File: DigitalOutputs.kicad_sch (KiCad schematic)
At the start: 2 parts, among them J3 DIGITAL_OUTPUTS

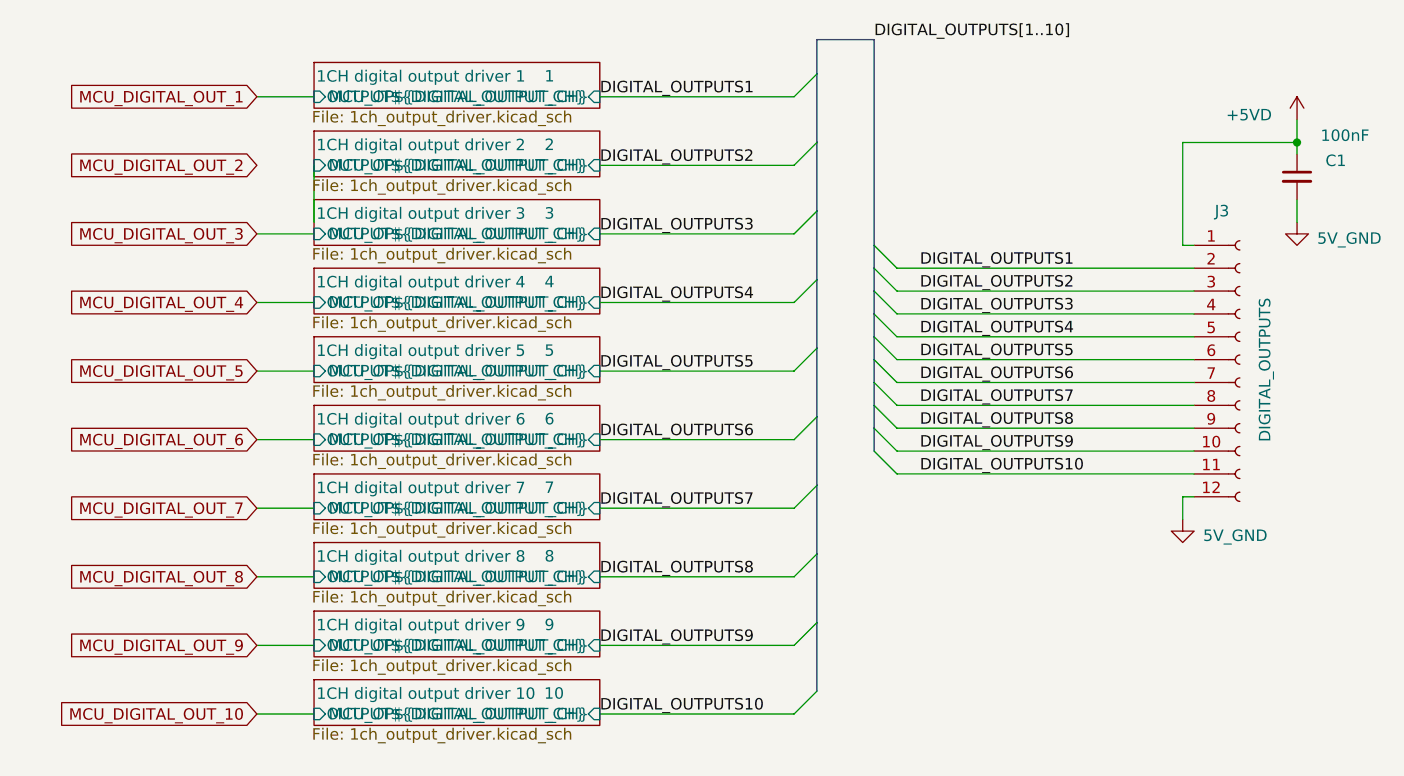
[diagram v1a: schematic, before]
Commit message: digital inputs section
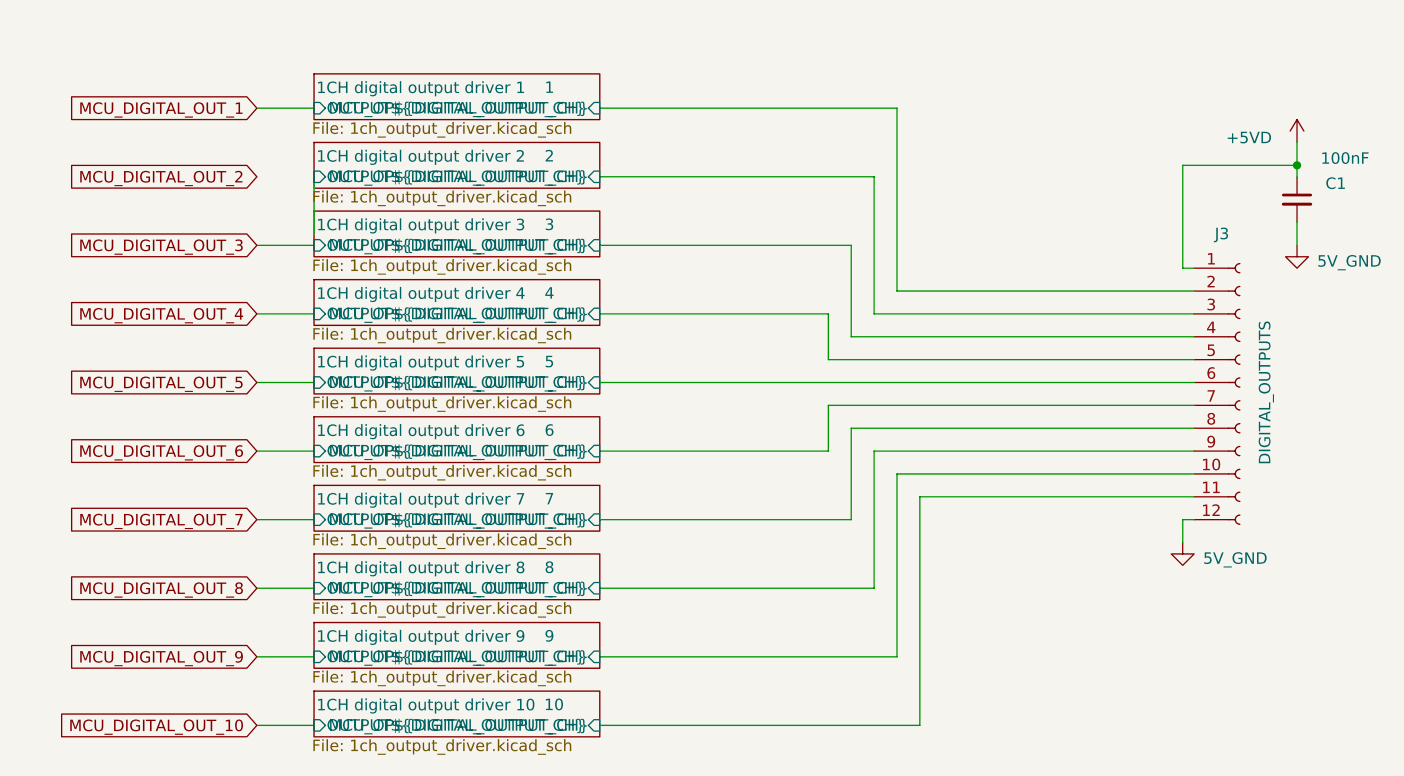
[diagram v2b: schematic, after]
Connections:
- net DIGITAL_OUTPUTS1 renamed 1CH digital output driver 1/OUTPUT${DIGITAL_OUTPUT_CH}
- net DIGITAL_OUTPUTS10 renamed 1CH digital output driver 10/OUTPUT${DIGITAL_OUTPUT_CH}
- net DIGITAL_OUTPUTS2 renamed 1CH digital output driver 2/OUTPUT${DIGITAL_OUTPUT_CH}
- net DIGITAL_OUTPUTS3 renamed 1CH digital output driver 3/OUTPUT${DIGITAL_OUTPUT_CH}
- net DIGITAL_OUTPUTS4 renamed 1CH digital output driver 4/OUTPUT${DIGITAL_OUTPUT_CH}
- net DIGITAL_OUTPUTS5 renamed 1CH digital output driver 5/OUTPUT${DIGITAL_OUTPUT_CH}
- net DIGITAL_OUTPUTS6 renamed 1CH digital output driver 6/OUTPUT${DIGITAL_OUTPUT_CH}
- net DIGITAL_OUTPUTS7 renamed 1CH digital output driver 7/OUTPUT${DIGITAL_OUTPUT_CH}
- net DIGITAL_OUTPUTS8 renamed 1CH digital output driver 8/OUTPUT${DIGITAL_OUTPUT_CH}
- net DIGITAL_OUTPUTS9 renamed 1CH digital output driver 9/OUTPUT${DIGITAL_OUTPUT_CH}
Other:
- moved on the sheet: C1, J3

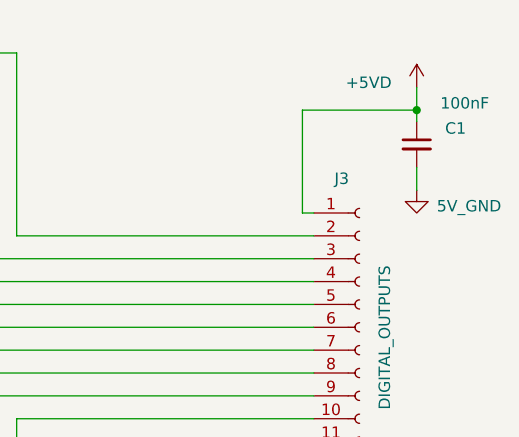
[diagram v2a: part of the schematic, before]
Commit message: Deleted stale test production files. Fixed up a bug with power isolation. Created some footprints for wire to board connectors although ran out of time to fix a bug where they do no lock in. Fixes to readme
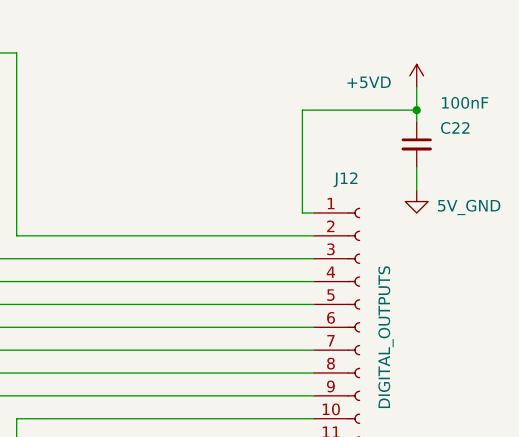
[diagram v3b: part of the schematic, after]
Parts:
- J12: renamed from J3; footprint (none) -> OSTVTerminalBlocks:Conn01x12
- renumbered C1 to C22
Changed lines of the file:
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@@
 		(on_board yes)
 		(dnp no)
-		(property "Reference" "C1"
+		(property "Reference" "C22"
 			(at 216.408 74.422 0)
 			(effects
@@
 			(project "Remora Nucleo F446ZE Hat"
 				(path "/5473abc6-7b93-43cc-a401-f691c4d7d7cf/a10f9653-3098-46b3-8571-958500eea49a"
-					(reference "C1")
+					(reference "C22")
 					(unit 1)
 				)
@@
 		(on_board yes)
 		(dnp no)
-		(property "Reference" "#PWR0136"
+		(property "Reference" "#PWR0135"
 			(at 199.39 120.65 0)
 			(effects
@@
 			(project "Remora Nucleo F446ZE Hat"
 				(path "/5473abc6-7b93-43cc-a401-f691c4d7d7cf/a10f9653-3098-46b3-8571-958500eea49a"
-					(reference "#PWR0136")
+					(reference "#PWR0135")
 					(unit 1)
 				)
@@
 		(on_board yes)
 		(dnp no)
-		(property "Reference" "#PWR0135"
+		(property "Reference" "#PWR0136"
 			(at 212.09 73.66 0)
 			(effects
@@
 			(project "Remora Nucleo F446ZE Hat"
 				(path "/5473abc6-7b93-43cc-a401-f691c4d7d7cf/a10f9653-3098-46b3-8571-958500eea49a"
-					(reference "#PWR0135")
+					(reference "#PWR0136")
 					(unit 1)
 				)
@@
 		(on_board yes)
 		(dnp no)
-		(property "Reference" "J3"
+		(property "Reference" "J12"
 			(at 202.946 80.01 0)
 			(effects
@@
 			)
 		)
-		(property "Footprint" ""
+		(property "Footprint" "OSTVTerminalBlocks:Conn01x12"
 			(at 205.74 96.52 0)
 			(effects
@@
 			(project "Remora Nucleo F446ZE Hat"
 				(path "/5473abc6-7b93-43cc-a401-f691c4d7d7cf/a10f9653-3098-46b3-8571-958500eea49a"
-					(reference "J3")
-					(unit 1)
-				)
+					(reference "J12")
+					(unit 1)
+				)

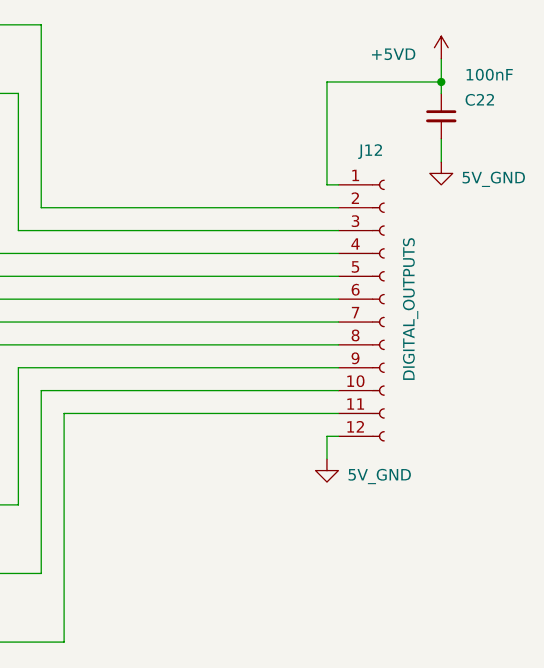
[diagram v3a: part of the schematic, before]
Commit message: restructured power supplies to enable Spindle DAC to be isolated. We now have the option of supplying two 24V inputs, one to power the nucleo and everything logic side and the other to power peripherals. Some testing will be required.
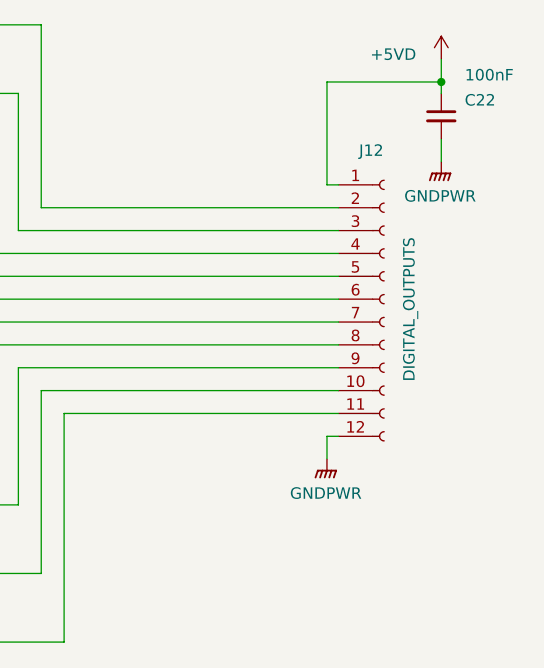
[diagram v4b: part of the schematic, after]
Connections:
- net 5V_GND renamed GNDPWR
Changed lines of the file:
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@@
 	)
 	(symbol
-		(lib_id "power:GND1")
+		(lib_id "power:GNDPWR")
 		(at 212.09 81.28 0)
 		(unit 1)
@@
 		(on_board yes)
 		(dnp no)
-		(property "Reference" "#PWR0137"
-			(at 212.09 87.63 0)
-			(effects
-				(font
-					(size 1.27 1.27)
-				)
-				(hide yes)
-			)
-		)
-		(property "Value" "5V_GND"
-			(at 221.488 83.058 0)
-			(effects
-				(font
-					(size 1.27 1.27)
-				)
-				(justify right)
+		(fields_autoplaced yes)
+		(property "Reference" "#PWR0117"
+			(at 212.09 86.36 0)
+			(effects
+				(font
+					(size 1.27 1.27)
+				)
+				(hide yes)
+			)
+		)
+		(property "Value" "GNDPWR"
+			(at 211.963 85.09 0)
+			(effects
+				(font
+					(size 1.27 1.27)
+				)
 			)
 		)
 		(property "Footprint" ""
+			(at 212.09 82.55 0)
+			(effects
+				(font
+					(size 1.27 1.27)
+				)
+				(hide yes)
+			)
+		)
+		(property "Datasheet" ""
+			(at 212.09 82.55 0)
+			(effects
+				(font
+					(size 1.27 1.27)
+				)
+				(hide yes)
+			)
+		)
+		(property "Description" "Power symbol creates a global label with name \"GNDPWR\" , global ground"
 			(at 212.09 81.28 0)
 			(effects
@@
 			)
 		)
-		(property "Datasheet" ""
-			(at 212.09 81.28 0)
-			(effects
-				(font
-					(size 1.27 1.27)
-				)
-				(hide yes)
-			)
-		)
-		(property "Description" "Power symbol creates a global label with name \"GND1\" , ground"
-			(at 212.09 81.28 0)
-			(effects
-				(font
-					(size 1.27 1.27)
-				)
-				(hide yes)
-			)
-		)
-		(pin "1"
-		)
-		(instances
-			(project "Remora Nucleo F446ZE Hat"
-				(path "/5473abc6-7b93-43cc-a401-f691c4d7d7cf/a10f9653-3098-46b3-8571-958500eea49a"
-					(reference "#PWR0137")
-					(unit 1)
-				)
-			)
-		)
-	)
-	(symbol
-		(lib_id "power:GND1")
-		(at 199.39 114.3 0)
-		(unit 1)
-		(exclude_from_sim no)
-		(in_bom yes)
-		(on_board yes)
-		(dnp no)
-		(property "Reference" "#PWR0135"
-			(at 199.39 120.65 0)
-			(effects
-				(font
-					(size 1.27 1.27)
-				)
-				(hide yes)
-			)
-		)
-		(property "Value" "5V_GND"
-			(at 205.232 116.078 0)
-			(effects
-				(font
-					(size 1.27 1.27)
-				)
-			)
-		)
-		(property "Footprint" ""
-			(at 199.39 114.3 0)
-			(effects
-				(font
-					(size 1.27 1.27)
-				)
-				(hide yes)
-			)
-		)
-		(property "Datasheet" ""
-			(at 199.39 114.3 0)
-			(effects
-				(font
-					(size 1.27 1.27)
-				)
-				(hide yes)
-			)
-		)
-		(property "Description" "Power symbol creates a global label with name \"GND1\" , ground"
-			(at 199.39 114.3 0)
-			(effects
-				(font
-					(size 1.27 1.27)
-				)
-				(hide yes)
-			)
-		)
-		(pin "1"
-		)
-		(instances
-			(project "Remora Nucleo F446ZE Hat"
-				(path "/5473abc6-7b93-43cc-a401-f691c4d7d7cf/a10f9653-3098-46b3-8571-958500eea49a"
-					(reference "#PWR0135")
+		(pin "1"
+		)
+		(instances
+			(project "Remora Nucleo F446ZE Hat"
+				(path "/5473abc6-7b93-43cc-a401-f691c4d7d7cf/a10f9653-3098-46b3-8571-958500eea49a"
+					(reference "#PWR0117")
 					(unit 1)
 				)
@@
 					(unit 1)
 				)
+			)
+		)
+	)
+	(symbol
+		(lib_id "power:GNDPWR")
+		(at 199.39 114.3 0)
+		(unit 1)
+		(exclude_from_sim no)
+		(in_bom yes)
+		(on_board yes)
+		(dnp no)
+		(fields_autoplaced yes)
+		(property "Reference" "#PWR0113"
+			(at 199.39 119.38 0)
+			(effects
+				(font
+					(size 1.27 1.27)
+				)
+				(hide yes)
+			)
+		)
+		(property "Value" "GNDPWR"
+			(at 199.263 118.11 0)
+			(effects
+				(font
+					(size 1.27 1.27)
+				)
+			)
+		)
+		(property "Footprint" ""
+			(at 199.39 115.57 0)
+			(effects
+				(font
+					(size 1.27 1.27)
+				)
+				(hide yes)
+			)
+		)
+		(property "Datasheet" ""
+			(at 199.39 115.57 0)
+			(effects
+				(font
+					(size 1.27 1.27)
+				)
+				(hide yes)
+			)
+		)
+		(property "Description" "Power symbol creates a global label with name \"GNDPWR\" , global ground"
+			(at 199.39 114.3 0)
+			(effects
+				(font
+					(size 1.27 1.27)
+				)
+				(hide yes)
+			)
+		)
+		(pin "1"
+		)
+		(instances
+			(project "Remora Nucleo F446ZE Hat"
+				(path "/5473abc6-7b93-43cc-a401-f691c4d7d7cf/a10f9653-3098-46b3-8571-958500eea49a"
+					(reference "#PWR0113")
+					(unit 1)
+				)

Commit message: Fixes to screw terminal footprints, updated BOM and included in project folder
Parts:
- J12: footprint OSTVTerminalBlocks:Conn01x12 -> EBWA_06_A:CONN_EBWA-12-A_ADM
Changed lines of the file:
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@@
 			)
 		)
-		(property "Footprint" "OSTVTerminalBlocks:Conn01x12"
+		(property "Footprint" "EBWA_06_A:CONN_EBWA-12-A_ADM"
 			(at 205.74 96.52 0)
 			(effects

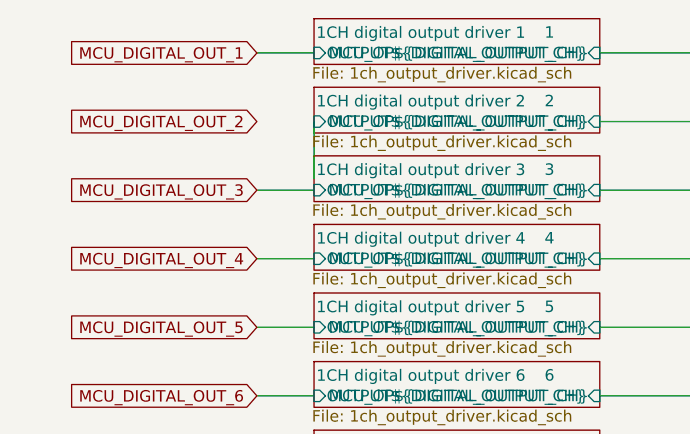
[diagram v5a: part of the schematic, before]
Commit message: Fixed bug with lack of pin header for CN11 and CN12. Addeded RPI header and aligned it, assigned some safe footprints
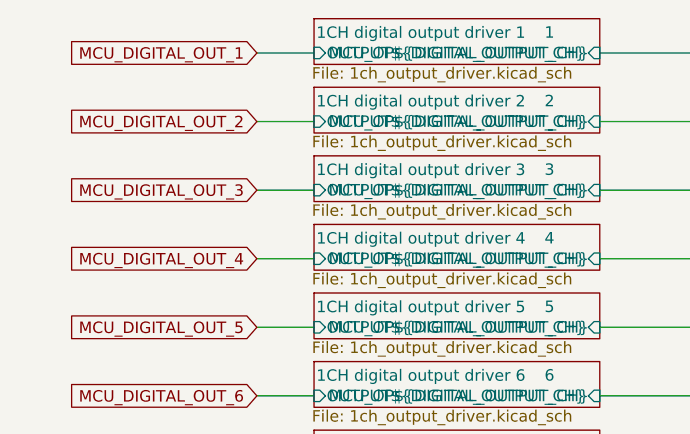
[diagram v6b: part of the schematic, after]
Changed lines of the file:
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@@
+	(wire
+		(pts
+			(xy 96.52 73.66) (xy 102.87 73.66)
+		)
+		(stroke
+			(width 0)
+			(type default)
+		)
+	)
 	(wire
 		(pts
@@
 		)
 		(stroke
-			(width 0)
-			(type default)
-		)
-	)
-	(wire
-		(pts
-			(xy 102.87 80.01) (xy 102.87 73.66)
-		)
-		(stroke

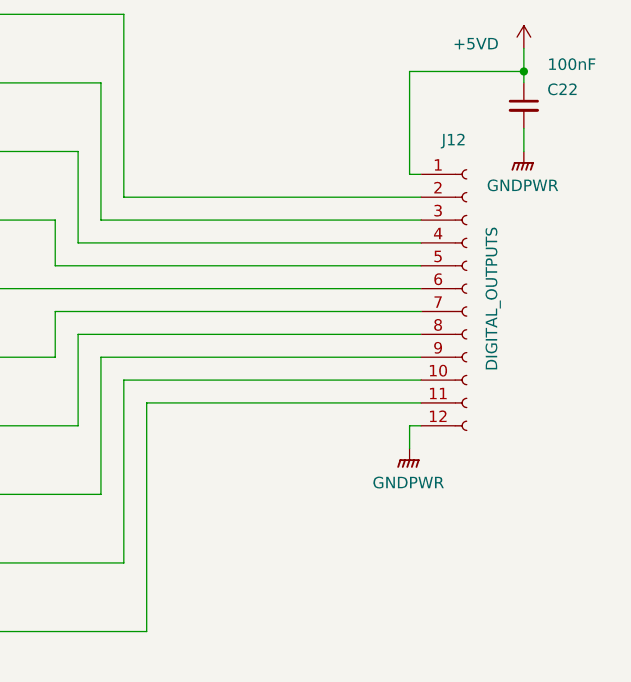
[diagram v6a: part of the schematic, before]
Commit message: updates to read me, marked V1 parts inactive and made start on board layout for initial test board. fixes to BOM to suit
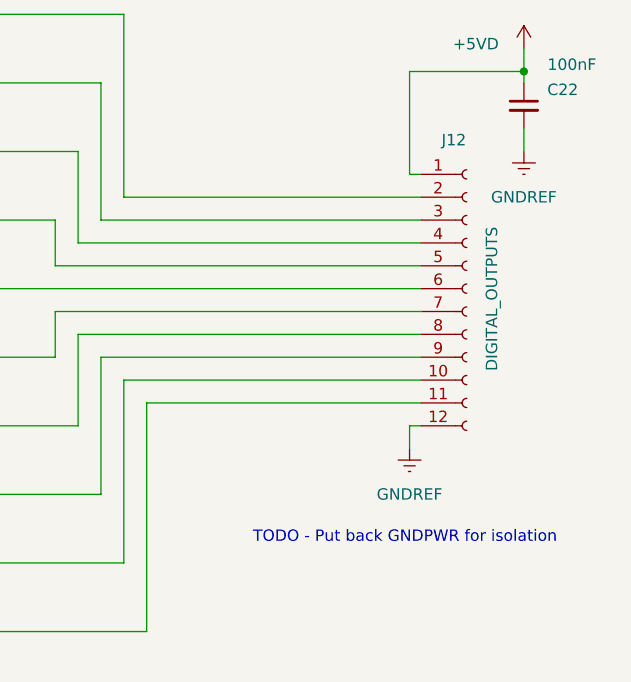
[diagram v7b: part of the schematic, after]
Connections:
- net GNDPWR renamed GNDREF
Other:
- note added: "TODO - Put back GNDPWR for isolation"
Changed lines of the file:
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@@
 	(generator_version "9.0")
 	(paper "A4")
+	(text "TODO - Put back GNDPWR for isolation\n"
+		(exclude_from_sim no)
+		(at 198.882 124.206 0)
+		(effects
+			(font
+				(size 1.27 1.27)
+			)
+		)
+	)
 	(junction
 		(at 212.09 72.39)
@@
 				(justify right)
 				(hide yes)
+			)
+		)
+	)
+	(symbol
+		(lib_id "power:GNDREF")
+		(at 199.39 114.3 0)
+		(unit 1)
+		(exclude_from_sim no)
+		(in_bom yes)
+		(on_board yes)
+		(dnp no)
+		(fields_autoplaced yes)
+		(property "Reference" "#PWR0117"
+			(at 199.39 120.65 0)
+			(effects
+				(font
+					(size 1.27 1.27)
+				)
+				(hide yes)
+			)
+		)
+		(property "Value" "GNDREF"
+			(at 199.39 119.38 0)
+			(effects
+				(font
+					(size 1.27 1.27)
+				)
+			)
+		)
+		(property "Footprint" ""
+			(at 199.39 114.3 0)
+			(effects
+				(font
+					(size 1.27 1.27)
+				)
+				(hide yes)
+			)
+		)
+		(property "Datasheet" ""
+			(at 199.39 114.3 0)
+			(effects
+				(font
+					(size 1.27 1.27)
+				)
+				(hide yes)
+			)
+		)
+		(property "Description" "Power symbol creates a global label with name \"GNDREF\" , reference supply ground"
+			(at 199.39 114.3 0)
+			(effects
+				(font
+					(size 1.27 1.27)
+				)
+				(hide yes)
+			)
+		)
+		(pin "1"
+		)
+		(instances
+			(project "Remora Nucleo F446ZE Hat"
+				(path "/5473abc6-7b93-43cc-a401-f691c4d7d7cf/a10f9653-3098-46b3-8571-958500eea49a"
+					(reference "#PWR0117")
+					(unit 1)
+				)
 			)
 		)
@@
 	)
 	(symbol
-		(lib_id "power:GNDPWR")
+		(lib_id "power:GNDREF")
 		(at 212.09 81.28 0)
 		(unit 1)
@@
 		(dnp no)
 		(fields_autoplaced yes)
-		(property "Reference" "#PWR0117"
+		(property "Reference" "#PWR0113"
+			(at 212.09 87.63 0)
+			(effects
+				(font
+					(size 1.27 1.27)
+				)
+				(hide yes)
+			)
+		)
+		(property "Value" "GNDREF"
 			(at 212.09 86.36 0)
 			(effects
@@
 					(size 1.27 1.27)
 				)
-				(hide yes)
-			)
-		)
-		(property "Value" "GNDPWR"
-			(at 211.963 85.09 0)
-			(effects
-				(font
-					(size 1.27 1.27)
-				)
 			)
 		)
 		(property "Footprint" ""
-			(at 212.09 82.55 0)
+			(at 212.09 81.28 0)
 			(effects
 				(font
@@
 		)
 		(property "Datasheet" ""
-			(at 212.09 82.55 0)
-			(effects
-				(font
-					(size 1.27 1.27)
-				)
-				(hide yes)
-			)
-		)
-		(property "Description" "Power symbol creates a global label with name \"GNDPWR\" , global ground"
 			(at 212.09 81.28 0)
 			(effects
@@
 			)
 		)
+		(property "Description" "Power symbol creates a global label with name \"GNDREF\" , reference supply ground"
+			(at 212.09 81.28 0)
+			(effects
+				(font
+					(size 1.27 1.27)
+				)
+				(hide yes)
+			)
+		)
 		(pin "1"
 		)
 		(instances
-			(project "Remora Nucleo F446ZE Hat"
+			(project ""
 				(path "/5473abc6-7b93-43cc-a401-f691c4d7d7cf/a10f9653-3098-46b3-8571-958500eea49a"
-					(reference "#PWR0117")
+					(reference "#PWR0113")
 					(unit 1)
 				)
@@
 					(unit 1)
 				)
-			)
-		)
-	)
-	(symbol
-		(lib_id "power:GNDPWR")
-		(at 199.39 114.3 0)
-		(unit 1)
-		(exclude_from_sim no)
-		(in_bom yes)
-		(on_board yes)
-		(dnp no)
-		(fields_autoplaced yes)
-		(property "Reference" "#PWR0113"
-			(at 199.39 119.38 0)
-			(effects
-				(font
-					(size 1.27 1.27)
-				)
-				(hide yes)
-			)
-		)
-		(property "Value" "GNDPWR"
-			(at 199.263 118.11 0)
-			(effects
-				(font
-					(size 1.27 1.27)
-				)
-			)
-		)
-		(property "Footprint" ""
-			(at 199.39 115.57 0)
-			(effects
-				(font
-					(size 1.27 1.27)
-				)
-				(hide yes)
-			)
-		)
-		(property "Datasheet" ""
-			(at 199.39 115.57 0)
-			(effects
-				(font
-					(size 1.27 1.27)
-				)
-				(hide yes)
-			)
-		)
-		(property "Description" "Power symbol creates a global label with name \"GNDPWR\" , global ground"
-			(at 199.39 114.3 0)
-			(effects
-				(font
-					(size 1.27 1.27)
-				)
-				(hide yes)
-			)
-		)
-		(pin "1"
-		)
-		(instances
-			(project "Remora Nucleo F446ZE Hat"
-				(path "/5473abc6-7b93-43cc-a401-f691c4d7d7cf/a10f9653-3098-46b3-8571-958500eea49a"
-					(reference "#PWR0113")
-					(unit 1)
-				)
